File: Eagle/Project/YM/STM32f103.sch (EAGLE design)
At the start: 56 parts, among them IC1 YM3812, IC10 LM358D, IC11 YM3014B, IC12 LM358D, IC13 YM3812, IC14 YM3014B, IC15 LM358D, IC3 BA033CC0T, IC4 LM2575-5.0S, IC5 YM3812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

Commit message: midi + optocoupler op blad 7. 3 nieuwe libraries.
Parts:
- added 4K7, 91: RES-0805-SMD, +HU-Lib:RES-0805-SMD
- added C36: (no value), Clean-Kong:C-EUC0603
- added C37: 1p5, Clean-Kong:C-EUC0603
- added D2: BAT20JFILM, BAT20JFILM:BAT20JFILM
- added J1: DIN5, SparkFun-Connectors:DIN5
- added Q1: 6N136SDM, 6N136SDM:6N136SDM
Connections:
- new net N$16: D2.A, J1.5, Q1.VF-
- new net N$17: 91.2, D2.C, Q1.VF+
- new net N$18: C36.1, J1.2
- new net N$19: 91.1, J1.4
- new net N$21: C37.2, Q1.VB
- net 5V: now also 4K7.2, Q1.VCC
- net GND: now also C36.2, C37.1, Q1.GND
- net USART-RX: now also 4K7.1, Q1.VO
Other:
- note added: "Julian Schotborgh MIDI aanlsuiting via optocoupler."
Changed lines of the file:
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@@
 <setting verticaltext="up"/>
 </settings>
-<grid distance="50" unitdist="mil" unit="mil" style="lines" multiple="1" display="no" altdistance="0.01" altunitdist="inch" altunit="inch"/>
+<grid distance="50" unitdist="mil" unit="mil" style="lines" multiple="1" display="yes" altdistance="0.01" altunitdist="inch" altunit="inch"/>
 <layers>
 <layer number="1" name="Top" color="4" fill="1" visible="no" active="no"/>
@@
 <part name="GND3" library="supply1" library_urn="urn:adsk.eagle:library:371" deviceset="GND" device=""/>
 <part name="JP2" library="adafruit" library_urn="urn:adsk.eagle:library:420" deviceset="PINHD-1X6" device="" package3d_urn="urn:adsk.eagle:package:6240711/1"/>
-<part name="FRAME7" library="frames" deviceset="A4L-LOC" device=""/>
 <part name="FRAME2" library="frames" deviceset="A4L-LOC" device=""/>
 <part name="FRAME1" library="frames" deviceset="A4L-LOC" device=""/>
@@
 <part name="GND33" library="supply1" library_urn="urn:adsk.eagle:library:371" deviceset="GND" device=""/>
 <part name="U1" library="stm32" deviceset="STM32F10XRXT6" device=""/>
+<part name="FRAME8" library="frames" deviceset="A4L-LOC" device=""/>
+<part name="J1" library="SparkFun-Connectors" library_urn="urn:adsk.eagle:library:513" deviceset="DIN5" device="" package3d_urn="urn:adsk.eagle:package:38294/1"/>
+<part name="91" library="+HU-Lib" deviceset="RES-0805-SMD" device=""/>
+<part name="D2" library="BAT20JFILM" deviceset="BAT20JFILM" device=""/>
+<part name="Q1" library="6N136SDM" deviceset="6N136SDM" device=""/>
+<part name="C36" library="Clean-Kong" deviceset="C-EU" device="C0603"/>
+<part name="4K7" library="+HU-Lib" deviceset="RES-0805-SMD" device=""/>
+<part name="C37" library="Clean-Kong" deviceset="C-EU" device="C0603" value="1p5"/>
 </parts>
 <sheets>
@@
 </sheet>
 <sheet>
+<description>MIDI INPUT</description>
 <plain>
+<text x="163.83" y="17.78" size="1.778" layer="91">Julian Schotborgh
+MIDI aanlsuiting via optocoupler.</text>
 </plain>
 <instances>
-<instance part="FRAME7" gate="G$1" x="0" y="0" smashed="yes">
+<instance part="FRAME8" gate="G$1" x="0" y="0" smashed="yes">
 <attribute name="DRAWING_NAME" x="217.17" y="15.24" size="2.54" layer="94"/>
 <attribute name="LAST_DATE_TIME" x="217.17" y="10.16" size="2.286" layer="94"/>
 <attribute name="SHEET" x="230.505" y="5.08" size="2.54" layer="94"/>
+</instance>
+<instance part="J1" gate="G$1" x="44.45" y="83.82" smashed="yes" rot="R270">
+<attribute name="NAME" x="38.862" y="83.82" size="1.778" layer="95" font="vector" rot="R270" align="bottom-center"/>
+<attribute name="VALUE" x="36.576" y="83.82" size="1.778" layer="96" font="vector" rot="R270" align="top-center"/>
+</instance>
+<instance part="91" gate="G$1" x="74.93" y="105.41" smashed="yes">
+<attribute name="NAME" x="71.12" y="106.9086" size="1.778" layer="95"/>
+<attribute name="VALUE" x="71.12" y="102.108" size="1.778" layer="96"/>
+</instance>
+<instance part="D2" gate="G$1" x="99.06" y="97.79" smashed="yes" rot="R90">
+<attribute name="NAME" x="96.518790625" y="97.30716875" size="1.77885" layer="95" rot="R180"/>
+<attribute name="VALUE" x="96.51916875" y="100.102159375" size="1.77858125" layer="96" rot="R180"/>
+</instance>
+<instance part="Q1" gate="G$1" x="124.46" y="96.52" smashed="yes">
+<attribute name="NAME" x="133.35" y="102.87" size="1.778" layer="95" align="center-left"/>
+<attribute name="VALUE" x="133.35" y="100.33" size="1.778" layer="96" align="center-left"/>
+</instance>
+<instance part="C36" gate="G$1" x="60.96" y="72.39" smashed="yes">
+<attribute name="NAME" x="62.484" y="72.771" size="1.778" layer="95"/>
+<attribute name="VALUE" x="62.484" y="67.691" size="1.778" layer="96"/>
+</instance>
+<instance part="4K7" gate="G$1" x="176.53" y="100.33" smashed="yes" rot="R90">
+<attribute name="NAME" x="177.8" y="99.2886" size="1.778" layer="95"/>
+<attribute name="VALUE" x="177.8" y="97.028" size="1.778" layer="96"/>
+</instance>
+<instance part="C37" gate="G$1" x="168.91" y="83.82" smashed="yes" rot="R180">
+<attribute name="NAME" x="171.704" y="82.931" size="1.778" layer="95"/>
+<attribute name="VALUE" x="171.704" y="85.471" size="1.778" layer="96"/>
 </instance>
 </instances>
@@
 </busses>
 <nets>
+<net name="N$19" class="0">
+<segment>
+<pinref part="J1" gate="G$1" pin="4"/>
+<wire x1="49.53" y1="76.2" x2="49.53" y2="67.31" width="0.1524" layer="91"/>
+<wire x1="49.53" y1="67.31" x2="25.4" y2="67.31" width="0.1524" layer="91"/>
+<wire x1="25.4" y1="67.31" x2="25.4" y2="105.41" width="0.1524" layer="91"/>
+<wire x1="25.4" y1="105.41" x2="69.85" y2="105.41" width="0.1524" layer="91"/>
+<pinref part="91" gate="G$1" pin="1"/>
+</segment>
+</net>
+<net name="N$17" class="0">
+<segment>
+<pinref part="Q1" gate="G$1" pin="VF+"/>
+<wire x1="115.57" y1="93.98" x2="124.46" y2="93.98" width="0.1524" layer="91"/>
+<wire x1="115.57" y1="105.41" x2="115.57" y2="93.98" width="0.1524" layer="91"/>
+<wire x1="80.01" y1="105.41" x2="99.06" y2="105.41" width="0.1524" layer="91"/>
+<pinref part="91" gate="G$1" pin="2"/>
+<pinref part="D2" gate="G$1" pin="C"/>
+<wire x1="99.06" y1="105.41" x2="115.57" y2="105.41" width="0.1524" layer="91"/>
+<wire x1="99.06" y1="100.33" x2="99.06" y2="105.41" width="0.1524" layer="91"/>
+<junction x="99.06" y="105.41"/>
+</segment>
+</net>
+<net name="N$16" class="0">
+<segment>
+<pinref part="J1" gate="G$1" pin="5"/>
+<pinref part="Q1" gate="G$1" pin="VF-"/>
+<wire x1="49.53" y1="91.44" x2="99.06" y2="91.44" width="0.1524" layer="91"/>
+<pinref part="D2" gate="G$1" pin="A"/>
+<wire x1="99.06" y1="91.44" x2="124.46" y2="91.44" width="0.1524" layer="91"/>
+<wire x1="99.06" y1="91.44" x2="99.06" y2="95.25" width="0.1524" layer="91"/>
+<junction x="99.06" y="91.44"/>
+</segment>
+</net>
+<net name="N$18" class="0">
+<segment>
+<pinref part="J1" gate="G$1" pin="2"/>
+<wire x1="54.61" y1="83.82" x2="60.96" y2="83.82" width="0.1524" layer="91"/>
+<wire x1="60.96" y1="83.82" x2="60.96" y2="74.93" width="0.1524" layer="91"/>
+<pinref part="C36" gate="G$1" pin="1"/>
+</segment>
+</net>
+<net name="GND" class="0">
+<segment>
+<pinref part="C36" gate="G$1" pin="2"/>
+<wire x1="60.96" y1="67.31" x2="60.96" y2="64.77" width="0.1524" layer="91"/>
+<label x="60.96" y="64.77" size="1.778" layer="95"/>
+</segment>
+<segment>
+<pinref part="Q1" gate="G$1" pin="GND"/>
+<wire x1="152.4" y1="88.9" x2="156.21" y2="88.9" width="0.1524" layer="91"/>
+<wire x1="156.21" y1="88.9" x2="156.21" y2="81.28" width="0.1524" layer="91"/>
+<pinref part="C37" gate="G$1" pin="1"/>
+<wire x1="156.21" y1="81.28" x2="168.91" y2="81.28" width="0.1524" layer="91"/>
+<wire x1="168.91" y1="81.28" x2="168.91" y2="74.93" width="0.1524" layer="91"/>
+<junction x="168.91" y="81.28"/>
+<label x="168.91" y="74.93" size="1.778" layer="95"/>
+</segment>
+</net>
+<net name="5V" class="0">
+<segment>
+<pinref part="Q1" gate="G$1" pin="VCC"/>
+<wire x1="152.4" y1="96.52" x2="154.94" y2="96.52" width="0.1524" layer="91"/>
+<wire x1="154.94" y1="96.52" x2="154.94" y2="107.95" width="0.1524" layer="91"/>
+<wire x1="154.94" y1="107.95" x2="176.53" y2="107.95" width="0.1524" layer="91"/>
+<pinref part="4K7" gate="G$1" pin="2"/>
+<wire x1="176.53" y1="105.41" x2="176.53" y2="107.95" width="0.1524" layer="91"/>
+<junction x="176.53" y="107.95"/>
+<label x="187.96" y="107.95" size="1.778" layer="95"/>
+<wire x1="176.53" y1="107.95" x2="190.5" y2="107.95" width="0.1524" layer="91"/>
+</segment>
+</net>
+<net name="USART-RX" class="0">
+<segment>
+<pinref part="Q1" gate="G$1" pin="VO"/>
+<wire x1="152.4" y1="91.44" x2="176.53" y2="91.44" width="0.1524" layer="91"/>
+<pinref part="4K7" gate="G$1" pin="1"/>
+<wire x1="176.53" y1="95.25" x2="176.53" y2="91.44" width="0.1524" layer="91"/>
+<junction x="176.53" y="91.44"/>
+<label x="177.8" y="91.44" size="1.778" layer="95"/>
+<wire x1="176.53" y1="91.44" x2="190.5" y2="91.44" width="0.1524" layer="91"/>
+</segment>
+</net>
+<net name="N$21" class="0">
+<segment>
+<pinref part="Q1" gate="G$1" pin="VB"/>
+<wire x1="152.4" y1="93.98" x2="168.91" y2="93.98" width="0.1524" layer="91"/>
+<pinref part="C37" gate="G$1" pin="2"/>
+<wire x1="168.91" y1="93.98" x2="168.91" y2="88.9" width="0.1524" layer="91"/>
+</segment>
+</net>
 </nets>
 </sheet>
@@
 </drawing>
 <compatibility>
+<note version="6.3" minversion="6.2.2" severity="warning">
+Since Version 6.2.2 text objects can contain more than one line,
+which will not be processed correctly with this version.
+</note>
 <note version="8.2" severity="warning">
 Since Version 8.2, EAGLE supports online libraries. The ids

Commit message: MIDI input andere weerstanden erin gedaan en wat layout aangepast. YM-klok aangemaakt, moet nog geriviewd worden.
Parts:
- removed 4K7, 91: RES-0805-SMD, +HU-Lib:RES-0805-SMD
- added C38: 4.7nF, Clean-Kong:C-EUC0603
- added CRYSTAL1: ABLS-3.579545MHZ-17-B-4-Y-T, ABLS-3.579545MHZ-17-B-4-Y-T:ABLS-3.579545MHZ-17-B-4-Y-T
- added R1: 91R, +HU-Lib:1K
- added R3, R4: 470R, +HU-Lib:1K
- added R5: 4k7, +HU-Lib:1K
- added U2: 74AC04MTC, 74AC04MTC:74AC04MTC
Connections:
- new net N$20: CRYSTAL1.2, R3.2, U2.A0
- new net N$22: CRYSTAL1.1, R4.2, U2.A2, U2.~O1
- new net N$23: C38.2, R3.1, U2.~O0
- new net N$24: C38.1, R4.1, U2.A1
- net 5V: now also R5.1, U2.VCC; no longer 4K7.2
- net GND: now also U2.GND
- net N$17: now also R1.2; no longer 91.2
- net N$19: now also R1.1; no longer 91.1
- net USART-RX: now also R5.2; no longer 4K7.1
- net YM-CLK-I: now also U2.~O2
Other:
- note added: "Julian Schotborgh Klok voor YM3812"

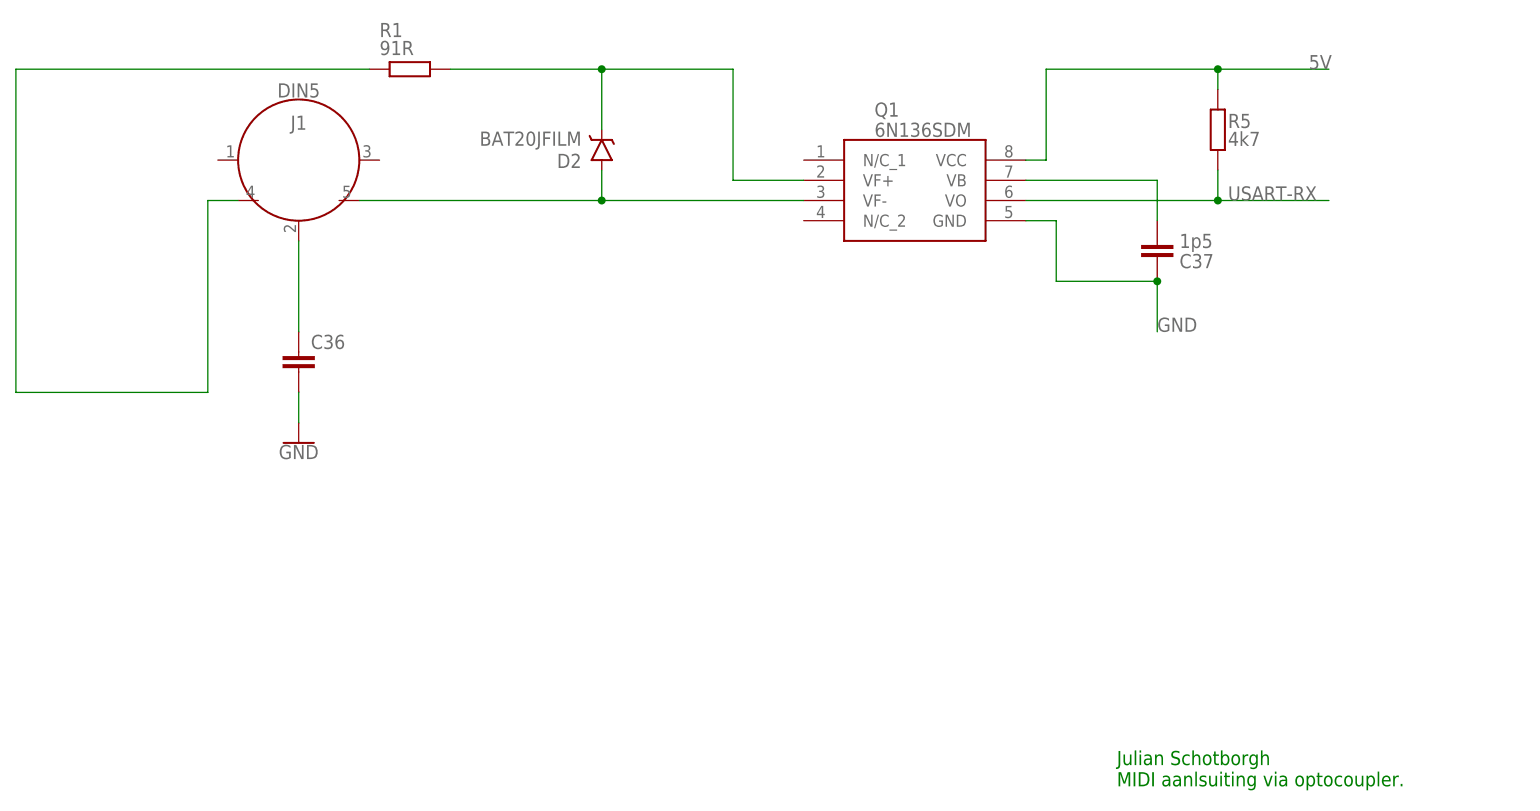
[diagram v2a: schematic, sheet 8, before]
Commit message: Review Ruben verwerkt: ontkoppel condensatoren voeding 6n136 en 7404.
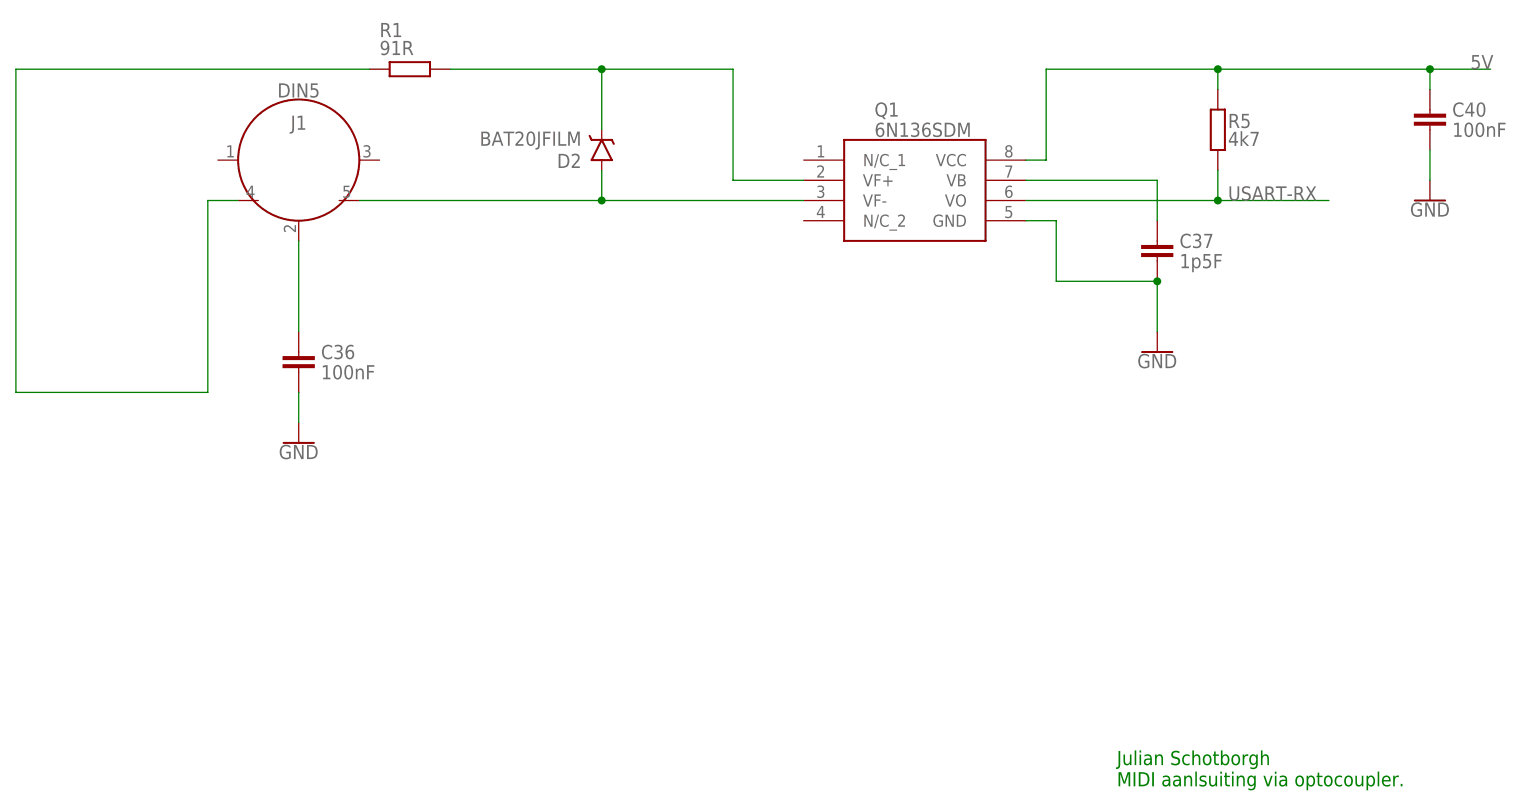
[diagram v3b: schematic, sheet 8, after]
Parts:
- added C39, C40: 100nF, Clean-Kong:C-EUC0603
- C36: value (none) -> 100nF
- C37: value 1p5 -> 1p5F
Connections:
- net 5V: now also C39.2, C40.2
- net GND: now also C39.1, C40.1
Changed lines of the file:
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@@
 <part name="D2" library="BAT20JFILM" deviceset="BAT20JFILM" device=""/>
 <part name="Q1" library="6N136SDM" deviceset="6N136SDM" device=""/>
-<part name="C36" library="Clean-Kong" deviceset="C-EU" device="C0603"/>
-<part name="C37" library="Clean-Kong" deviceset="C-EU" device="C0603" value="1p5"/>
+<part name="C36" library="Clean-Kong" deviceset="C-EU" device="C0603" value="100nF"/>
+<part name="C37" library="Clean-Kong" deviceset="C-EU" device="C0603" value="1p5F"/>
 <part name="FRAME7" library="frames" deviceset="A4L-LOC" device=""/>
 <part name="C38" library="Clean-Kong" deviceset="C-EU" device="C0603" value="4.7nF"/>
@@
 <part name="R1" library="+HU-Lib" deviceset="1K" device="" value="91R"/>
 <part name="R5" library="+HU-Lib" deviceset="1K" device="" value="4k7"/>
+<part name="C39" library="Clean-Kong" deviceset="C-EU" device="C0603" value="100nF"/>
+<part name="C40" library="Clean-Kong" deviceset="C-EU" device="C0603" value="100nF"/>
+<part name="GND40" library="SparkFun-PowerSymbols" library_urn="urn:adsk.eagle:library:530" deviceset="GND" device=""/>
+<part name="GND41" library="SparkFun-PowerSymbols" library_urn="urn:adsk.eagle:library:530" deviceset="GND" device=""/>
+<part name="GND42" library="SparkFun-PowerSymbols" deviceset="GND" device=""/>
 </parts>
 <sheets>
@@
 </instance>
 <instance part="C38" gate="G$1" x="63.5" y="102.87" smashed="yes" rot="R180">
-<attribute name="NAME" x="66.294" y="101.981" size="1.778" layer="95"/>
-<attribute name="VALUE" x="66.294" y="104.521" size="1.778" layer="96"/>
+<attribute name="NAME" x="66.294" y="104.521" size="1.778" layer="95"/>
+<attribute name="VALUE" x="66.294" y="101.981" size="1.778" layer="96"/>
 </instance>
 <instance part="U2" gate="G$1" x="111.76" y="107.95" smashed="yes">
@@
 <attribute name="NAME" x="80.01" y="96.7486" size="1.778" layer="95"/>
 <attribute name="VALUE" x="80.01" y="94.488" size="1.778" layer="96"/>
+</instance>
+<instance part="C39" gate="G$1" x="151.13" y="102.87" smashed="yes" rot="R180">
+<attribute name="NAME" x="153.924" y="104.521" size="1.778" layer="95"/>
+<attribute name="VALUE" x="153.924" y="101.981" size="1.778" layer="96"/>
+</instance>
+<instance part="GND42" gate="1" x="151.13" y="93.98" smashed="yes">
+<attribute name="VALUE" x="151.13" y="93.726" size="1.778" layer="96" align="top-center"/>
 </instance>
 </instances>
@@
 <wire x1="151.13" y1="107.95" x2="151.13" y2="114.3" width="0.1524" layer="91"/>
 <label x="151.13" y="113.03" size="1.778" layer="95"/>
+<pinref part="C39" gate="G$1" pin="2"/>
+<junction x="151.13" y="107.95"/>
 </segment>
 </net>
@@
 <wire x1="102.87" y1="92.71" x2="102.87" y2="88.9" width="0.1524" layer="91"/>
 <pinref part="GND39" gate="1" pin="GND"/>
+</segment>
+<segment>
+<pinref part="C39" gate="G$1" pin="1"/>
+<wire x1="151.13" y1="100.33" x2="151.13" y2="96.52" width="0.1524" layer="91"/>
+<pinref part="GND42" gate="1" pin="GND"/>
 </segment>
 </net>
@@
 </instance>
 <instance part="C36" gate="G$1" x="60.96" y="72.39" smashed="yes">
-<attribute name="NAME" x="62.484" y="72.771" size="1.778" layer="95"/>
-<attribute name="VALUE" x="62.484" y="67.691" size="1.778" layer="96"/>
+<attribute name="NAME" x="63.754" y="71.501" size="1.778" layer="95"/>
+<attribute name="VALUE" x="63.754" y="68.961" size="1.778" layer="96"/>
 </instance>
 <instance part="C37" gate="G$1" x="168.91" y="83.82" smashed="yes" rot="R180">
-<attribute name="NAME" x="171.704" y="82.931" size="1.778" layer="95"/>
-<attribute name="VALUE" x="171.704" y="85.471" size="1.778" layer="96"/>
+<attribute name="NAME" x="171.704" y="85.471" size="1.778" layer="95"/>
+<attribute name="VALUE" x="171.704" y="82.931" size="1.778" layer="96"/>
 </instance>
 <instance part="GND38" gate="1" x="60.96" y="60.96" smashed="yes">
@@
 <attribute name="NAME" x="177.8" y="100.5586" size="1.778" layer="95"/>
 <attribute name="VALUE" x="177.8" y="98.298" size="1.778" layer="96"/>
+</instance>
+<instance part="C40" gate="G$1" x="203.2" y="100.33" smashed="yes" rot="R180">
+<attribute name="NAME" x="205.994" y="101.981" size="1.778" layer="95"/>
+<attribute name="VALUE" x="205.994" y="99.441" size="1.778" layer="96"/>
+</instance>
+<instance part="GND40" gate="1" x="168.91" y="72.39" smashed="yes">
+<attribute name="VALUE" x="168.91" y="72.136" size="1.778" layer="96" align="top-center"/>
+</instance>
+<instance part="GND41" gate="1" x="203.2" y="91.44" smashed="yes">
+<attribute name="VALUE" x="203.2" y="91.186" size="1.778" layer="96" align="top-center"/>
 </instance>
 </instances>
@@
 <wire x1="168.91" y1="81.28" x2="168.91" y2="74.93" width="0.1524" layer="91"/>
 <junction x="168.91" y="81.28"/>
-<label x="168.91" y="74.93" size="1.778" layer="95"/>
+<pinref part="GND40" gate="1" pin="GND"/>
+</segment>
+<segment>
+<pinref part="C40" gate="G$1" pin="1"/>
+<wire x1="203.2" y1="97.79" x2="203.2" y2="93.98" width="0.1524" layer="91"/>
+<pinref part="GND41" gate="1" pin="GND"/>
 </segment>
 </net>
@@
 <wire x1="152.4" y1="96.52" x2="154.94" y2="96.52" width="0.1524" layer="91"/>
 <wire x1="154.94" y1="96.52" x2="154.94" y2="107.95" width="0.1524" layer="91"/>
+<label x="208.28" y="107.95" size="1.778" layer="95"/>
 <wire x1="154.94" y1="107.95" x2="176.53" y2="107.95" width="0.1524" layer="91"/>
+<wire x1="176.53" y1="107.95" x2="203.2" y2="107.95" width="0.1524" layer="91"/>
+<pinref part="R5" gate="G$1" pin="1"/>
+<wire x1="203.2" y1="107.95" x2="210.82" y2="107.95" width="0.1524" layer="91"/>
 <wire x1="176.53" y1="105.41" x2="176.53" y2="107.95" width="0.1524" layer="91"/>
 <junction x="176.53" y="107.95"/>
-<label x="187.96" y="107.95" size="1.778" layer="95"/>
-<wire x1="176.53" y1="107.95" x2="190.5" y2="107.95" width="0.1524" layer="91"/>
-<pinref part="R5" gate="G$1" pin="1"/>
+<pinref part="C40" gate="G$1" pin="2"/>
+<wire x1="203.2" y1="105.41" x2="203.2" y2="107.95" width="0.1524" layer="91"/>
+<junction x="203.2" y="107.95"/>
 </segment>
 </net>
@@
 <pinref part="Q1" gate="G$1" pin="VO"/>
 <wire x1="152.4" y1="91.44" x2="176.53" y2="91.44" width="0.1524" layer="91"/>
+<label x="177.8" y="91.44" size="1.778" layer="95"/>
+<pinref part="R5" gate="G$1" pin="2"/>
+<wire x1="176.53" y1="91.44" x2="190.5" y2="91.44" width="0.1524" layer="91"/>
 <wire x1="176.53" y1="95.25" x2="176.53" y2="91.44" width="0.1524" layer="91"/>
 <junction x="176.53" y="91.44"/>
-<label x="177.8" y="91.44" size="1.778" layer="95"/>
-<wire x1="176.53" y1="91.44" x2="190.5" y2="91.44" width="0.1524" layer="91"/>
-<pinref part="R5" gate="G$1" pin="2"/>
-</segment>
-</net>
+</segment>
+</net>

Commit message: USB CONN
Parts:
- removed C34: 100UF, +HU-Lib:100UF
- removed C35: 330UF, +HU-Lib:330UF
- removed D1: 1N5819-B, diode:1N5819-B
- removed IC4: LM2575-5.0S, lm2575:LM2575-5.0S
- removed L1: 330UH, +HU-Lib:330UH
- added J2: (no value), LDO:CON-USB-B
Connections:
- removed net 12V: C34.1, IC4.VIN
- removed net N$15: D1.C, IC4.OUT, L1.P$2
- net 5V: now also J2.1; no longer C35.1, IC4.FB, L1.P$1
- net GND: now also J2.4; no longer C34.2, C35.2, D1.A, IC4.GND, IC4.OFF
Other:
- moved on the sheet: C32, C33, IC3
